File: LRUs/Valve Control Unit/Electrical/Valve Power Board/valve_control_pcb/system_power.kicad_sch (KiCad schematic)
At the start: 50 parts, among them J10 Conn_01x02_Pin, J11 01x02_PinHeader, U13 AMS1117-3.3, U14 TPS62933P, U15 TPS2116DRL, U16 TPS22810DBV, U17 AMS1117-3.3, U18 TPS22810DBV

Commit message: Commit valve board updates
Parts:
- removed C51, C56: 10uF, Capacitor_Tantalum_SMD:CP_EIA-3216-18_Kemet-A, symbol Device:C_Polarized_Small_US
- removed C54, C55: 1uF, Capacitor_SMD:C_0805_2012Metric, symbol Device:C_Small_US
- removed TP91, TP92, TP93, TP94, TP95: TestPoint, TestPoint:TestPoint_Pad_D2.0mm, symbol Connector:TestPoint
- removed U13: AMS1117-3.3, Package_TO_SOT_SMD:SOT-223-3_TabPin2, symbol Regulator_Linear:AMS1117-3.3
- added TP102, TP103, TP104, TP105, TP106, TP107, TP108, TP109, TP110: TestPoint, TestPoint:TestPoint_Pad_D2.0mm, symbol Connector:TestPoint
- C50, C52: Footprint_Size (none) -> 7343
- C53, C57, C58: Footprint_Size (none) -> 0402
- C59, C60, C65: Footprint_Size (none) -> 3216
- C61, C63: Footprint_Size (none) -> 0805
- C62, C64, D29, R107, R108, R109, R110, R111, R112, R113, R114, R115, R116, R117, R118, R119, R121, R123, R124, R125: Footprint_Size (none) -> 0603
- L1: Footprint_Size (none) -> XAL6060
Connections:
- net 5V_MAIN_PG: now also TP106.1
- net V-3P3_LDO: now also TP107.1
- net V-5P0_BUCK: now also TP105.1
- net VBUS: now also TP102.1
- net VEN: now also TP103.1
- net VFB: now also TP104.1
- net 3V3_USB: now reaches U15.6 (VIN2)
- net at R117.1, R120.2, U15.2 (VOUT)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: now also TP108.1
- net at C62.1, U16.4 (CT): now also TP109.1
- net at C64.1, U18.4 (CT): now also TP110.1
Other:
- note added: "SYSTEM POWER"
- note added: "lower threshold for switch to main board rail: 3V"
- note removed: "Test Points & LEDs"
- note removed: "lower threshold for switch to main board GSE: 3V"
- title: (none) -> SYSTEM POWER
- moved on the sheet: C62, C64, D29, R111, R112, R114, R118, R119, R124, R125, U18

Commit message: Commit da changes
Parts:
- removed C50, C52: 10uF, Capacitor_Tantalum_SMD:CP_EIA-7343-31_Kemet-D, symbol Device:C_Polarized_Small_US
- removed C53, C57, C58: 100nF, Capacitor_SMD:C_0402_1005Metric, symbol Device:C_Small_US
- removed C59, C60, C65: 10uF, Capacitor_Tantalum_SMD:CP_EIA-3216-18_Kemet-A, symbol Device:C_Polarized_Small_US
- removed C61, C63: 1uF, Capacitor_SMD:C_0805_2012Metric, symbol Device:C_Small_US
- removed C62, C64: 10nF, Capacitor_SMD:C_0603_1608Metric, symbol Device:C_Small_US
- removed D29: RED, LED_SMD:LED_0603_1608Metric, symbol Device:LED
- removed J10: Conn_01x02_Pin, Connector_PinHeader_2.54mm:PinHeader_1x02_P2.54mm_Vertical, symbol Connector:Conn_01x02_Pin
- removed J11: 01x02_PinHeader, Connector_PinHeader_2.54mm:PinHeader_1x02_P2.54mm_Vertical, symbol Connector:Conn_01x02_Pin
- removed L1: 15uH, Inductor_SMD:L_Coilcraft_XAL6060-XXX, symbol Device:L
- removed R107: 220k, Resistor_SMD:R_0603_1608Metric, symbol Device:R_Small_US
- removed R108, R115: 20k, Resistor_SMD:R_0603_1608Metric, symbol Device:R_Small_US
- removed R109: 9.1k, Resistor_SMD:R_0603_1608Metric, symbol Device:R_Small_US
- removed R110, R123: 51k, Resistor_SMD:R_0603_1608Metric, symbol Device:R_Small_US
- removed R111, R112: 2.2k, Resistor_SMD:R_0603_1608Metric, symbol Device:R_Small_US
- removed R113: 0, Resistor_SMD:R_0603_1608Metric, symbol Device:R_Small_US
- removed R114, R117: 47k, Resistor_SMD:R_0603_1608Metric, symbol Device:R_Small_US
- removed R116, R124, R125: 10k, Resistor_SMD:R_0603_1608Metric, symbol Device:R_Small_US
- removed R118: 68k, Resistor_SMD:R_0603_1608Metric, symbol Device:R_Small_US
- removed R119: 13k, Resistor_SMD:R_0603_1608Metric, symbol Device:R_Small_US
- removed R120, R122: 150k, Resistor_SMD:R_0603_1608Metric, symbol Device:R_Small_US
- removed R121: 100k, Resistor_SMD:R_0603_1608Metric, symbol Device:R_Small_US
- removed TP102, TP103, TP104, TP105, TP106, TP107, TP108, TP109, TP110: TestPoint, TestPoint:TestPoint_Pad_D2.0mm, symbol Connector:TestPoint
- removed U14: TPS62933P, Package_TO_SOT_SMD:SOT-583-8, symbol Regulator_Switching:TPS62933P
- removed U15: TPS2116DRL, Package_TO_SOT_SMD:SOT-583-8, symbol Power_Management:TPS2116DRL
- removed U16, U18: TPS22810DBV, Package_TO_SOT_SMD:SOT-23-6, symbol Power_Management:TPS22810DBV
- removed U17: AMS1117-3.3, Package_TO_SOT_SMD:SOT-223-3_TabPin2, symbol Regulator_Linear:AMS1117-3.3
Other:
- added sheet LDO 3V3 (ldo_3V3.kicad_sch)
- added sheet LSW 3V3 (lsw_3V3.kicad_sch)
- added sheet LSW 5V (lsw_5V.kicad_sch)
- added sheet MUX 3V3 (mux_3V3.kicad_sch)
- added sheet System 5V (system_5V.kicad_sch)
- note added: "20"
- note added: "22"
- note added: "32"
- note added: "AMS1117"
- note added: "TPS2116DRL"
- note added: "TPS22810DBV"
- note added: "TPS62933P"
- note removed: "1.2MHz"
- note removed: "30% ripple @ 500mA"
- note removed: "3V3 Inhibit"
- note removed: "5V Inhibit"
- note removed: "UVLO RISING: 3.08V UVLO FALLING: 2.83V"
- note removed: "UVLO RISING: 4.85V UVLO FALLING: 4.45V"
- note removed: "VEN = 0.1703*VIN+0.08904"
- note removed: "Vout = 0.8*(1+68k/13k) Vout = 4.98V"
- note removed: "Vstart = 7V Vstop = 6.4V"
- note removed: "lower threshold for switch to main board rail: 3V"

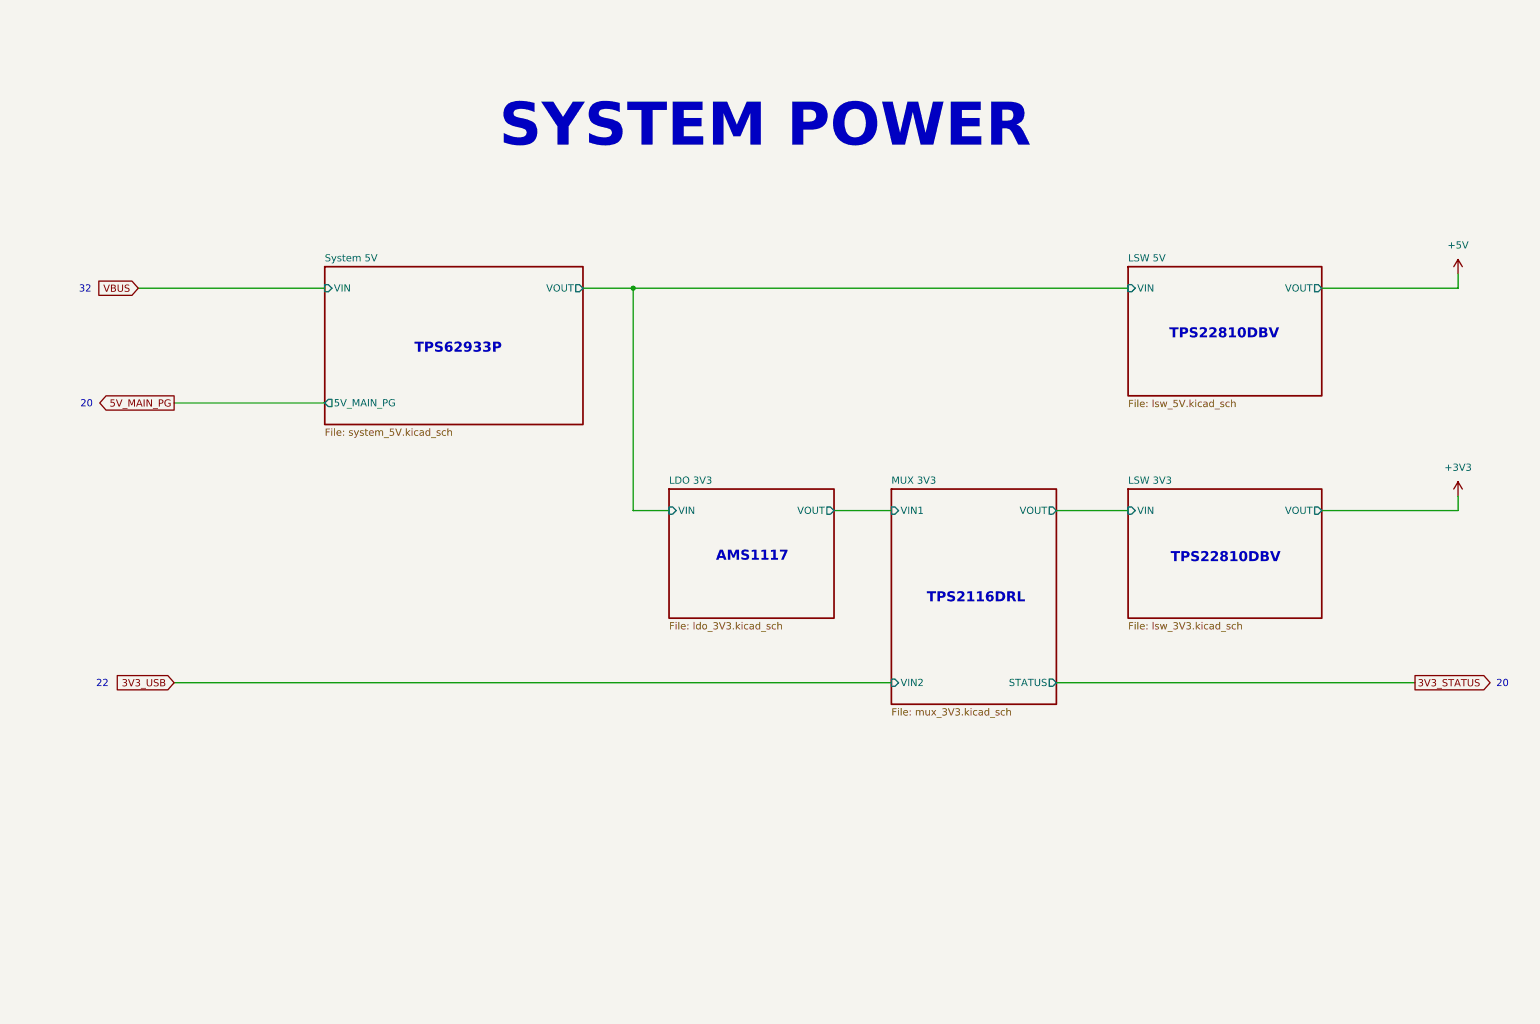
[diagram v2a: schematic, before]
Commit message: Major changes due to architecture
Added battery muxing for valve power, igniter system, and separate system battery for control electronics
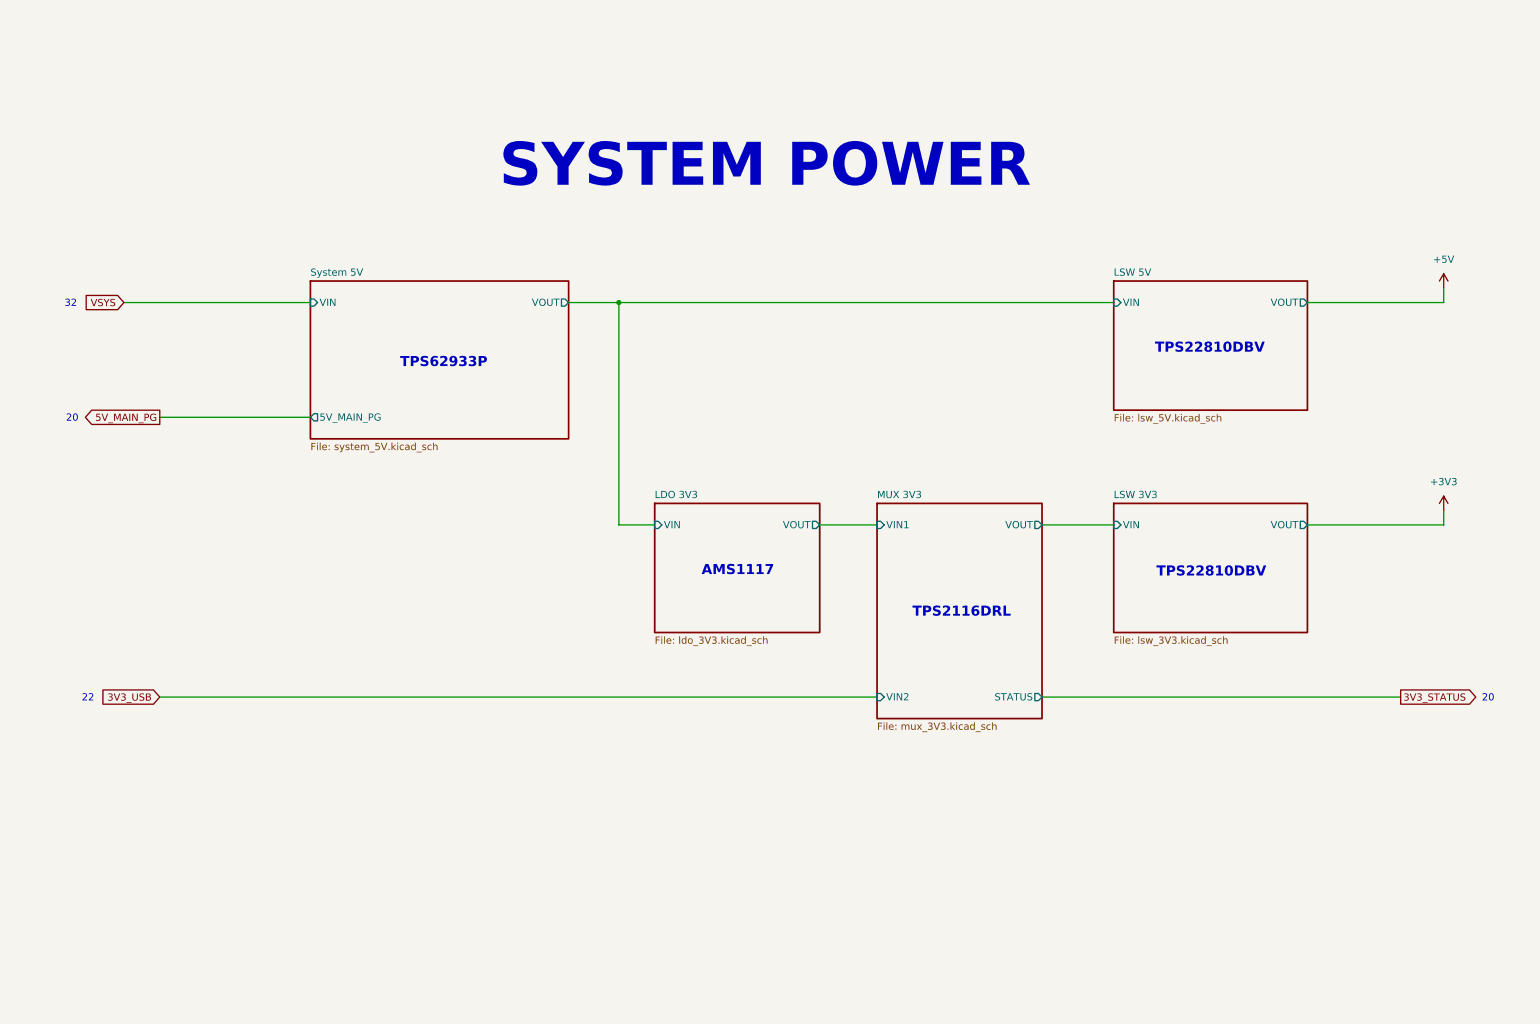
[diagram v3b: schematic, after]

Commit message: Major changes
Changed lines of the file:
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@@
 	(title_block
 		(title "SYSTEM POWER")
-		(date "2026-10-07")
+		(date "2026-10-08")
 		(rev "A")
 	)
@@
 	(text "SYSTEM POWER"
 		(exclude_from_sim no)
-		(at 146.558 44.45 0)
+		(at 146.558 28.448 0)
 		(effects
 			(font
